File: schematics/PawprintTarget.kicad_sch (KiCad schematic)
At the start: 47 parts, among them J1 Conn_01x15, J2 Conn_01x15, J4 RJ45, J5 RJ45, J8 Conn_01x04_Pin, J9 Conn_01x04_Pin, Q1 IRF540N, Q2 IRF540N, SW1 SW_DIP_x04, SW2 SW_DIP_x04, U1 MAX485E, U2 TSOP38G36, U3 Mini360

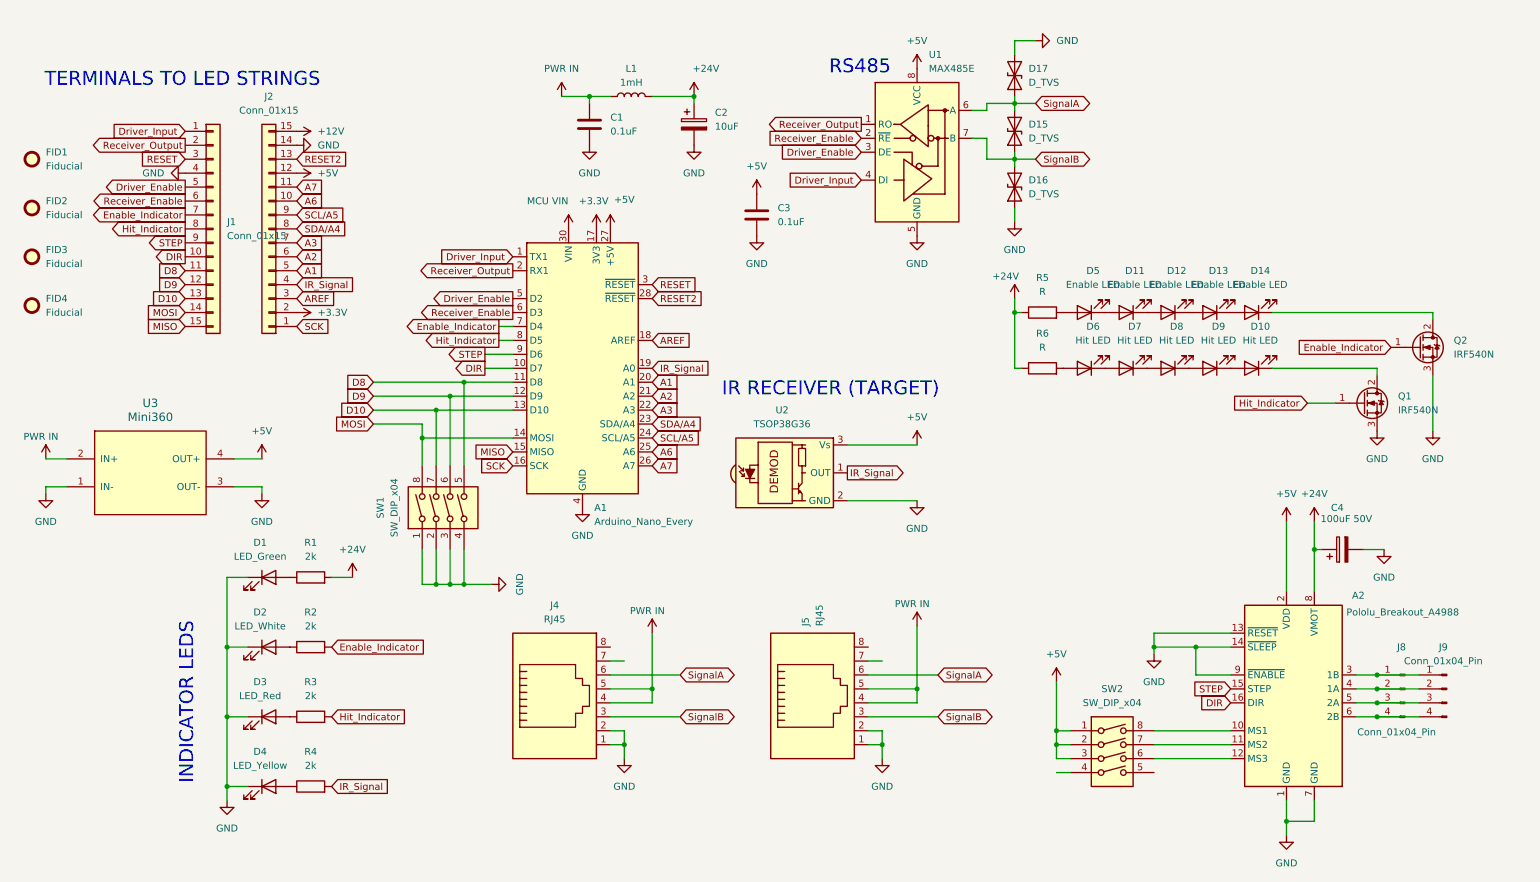
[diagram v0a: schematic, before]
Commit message: Component placements finished
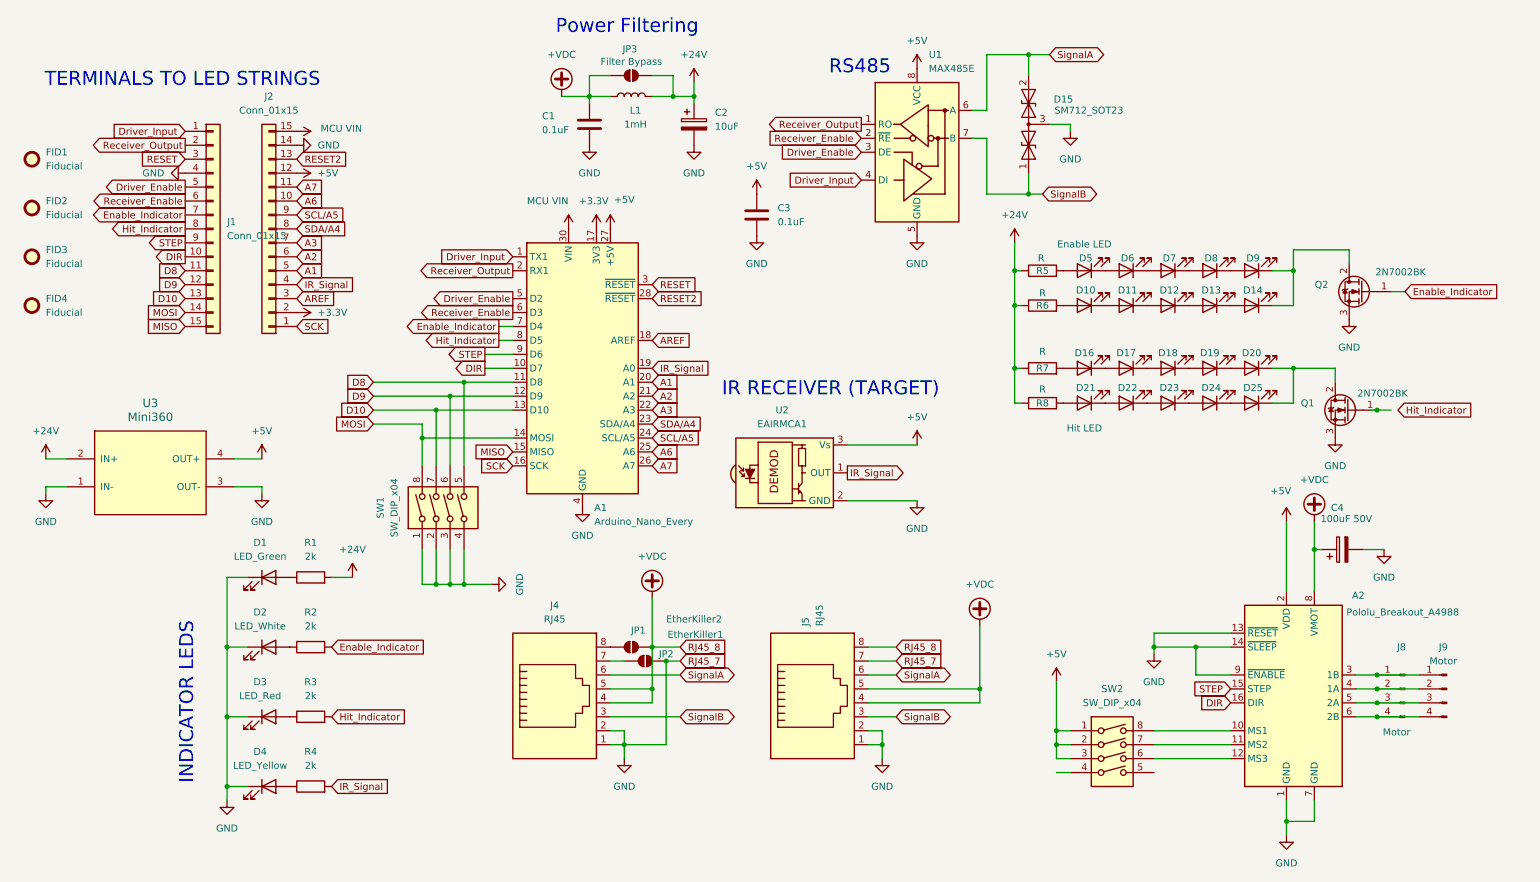
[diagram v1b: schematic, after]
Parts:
- removed D15, D16, D17: D_TVS, symbol Device:D_TVS
- added D10, D11, D12, D13, D14: Enable LED, LED_SMD:LED_1206_3216Metric, symbol Device:LED
- added D15: SM712_SOT23, Package_TO_SOT_SMD:SOT-23, symbol Diode:SM712_SOT23
- added D21, D22, D23, D24, D25: Hit LED, LED_SMD:LED_1206_3216Metric, symbol Device:LED
- added JP1: EtherKiller1, Jumper:SolderJumper-2_P1.3mm_Open_TrianglePad1.0x1.5mm, symbol Jumper:SolderJumper_2_Open
- added JP2: EtherKiller2, Jumper:SolderJumper-2_P1.3mm_Open_TrianglePad1.0x1.5mm, symbol Jumper:SolderJumper_2_Open
- added JP3: Filter Bypass, Jumper:SolderJumper-2_P1.3mm_Open_TrianglePad1.0x1.5mm, symbol Jumper:SolderJumper_2_Open
- added R6, R8: R, Resistor_SMD:R_0603_1608Metric, symbol Device:R
- C1, C3: footprint Capacitor_THT:C_Disc_D3.0mm_W2.0mm_P2.50mm -> Capacitor_SMD:C_0805_2012Metric
- C2: footprint Capacitor_THT:CP_Radial_D5.0mm_P2.00mm -> Capacitor_SMD:C_1206_3216Metric
- J8: value Conn_01x04_Pin -> Motor
- J9: value Conn_01x04_Pin -> Motor; footprint Connector_PinSocket_2.54mm:PinSocket_1x04_P2.54mm_Vertical -> Connector_JST:JST_PH_B4B-PH-K_1x04_P2.00mm_Vertical
- L1: footprint Inductor_THT:L_Radial_D9.5mm_P5.00mm_Fastron_07HVP -> Mini360_step-down:Inductor_SDR1307
- Q1, Q2: value IRF540N -> 2N7002BK; footprint Package_TO_SOT_THT:TO-220-3_Vertical -> Package_TO_SOT_SMD:SOT-23-3
- R1, R2, R3, R4: footprint Resistor_SMD:R_1210_3225Metric -> Resistor_SMD:R_0603_1608Metric
- U2: value TSOP38G36 -> EAIRMCA1; footprint OptoDevice:Vishay_MINICAST-3Pin -> OptoDevice:Vishay_MOLD-3Pin
- renumbered D6 to D16, D7 to D17, D8 to D18, D9 to D19, D10 to D20, D11 to D6, D12 to D7, D13 to D8, D14 to D9, R6 to R7
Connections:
- net +12V is gone; now on net MCU VIN: J2.15 (Pin_15)
- net +24V: now also U3.2 (IN+), JP3.2 (B), R6.1, R8.1; no longer A2.8 (VMOT), C4.1
- net GND: now also J5.7, D15.3 (common), JP1.2 (B)
- net Hit_Indicator: no longer Q1.1 (G)
- net SignalA: now also D15.2 (A2)
- net SignalB: now also D15.1 (A1)
- net at J4.7: now also JP1.1 (A)
- net at J4.8: now also JP2.1 (A)
- net at D9.1 (K), Q2.2 (D): now also D14.1 (K)
- net +VDC: now reaches J5.8
- net +VDC: now also A2.8 (VMOT), C1.1, C4.1, J4.4, J4.5, J5.4, J5.5, L1.1, JP2.2 (B), JP3.1 (A)
- net at D20.1 (K), Q1.2 (D): now also D25.1 (K)
- removed net PWR IN: C1.1, J4.4, J4.5, J5.4, J5.5, L1.1, U3.2 (IN+)
- new net: D12.1 (K), D13.2 (A)
- new net: D11.1 (K), D12.2 (A)
- new net: D23.1 (K), D24.2 (A)
- new net: D22.1 (K), D23.2 (A)
- new net: D21.1 (K), D22.2 (A)
- new net: D21.2 (A), R8.2
- new net: D10.2 (A), R6.2
- new net: D10.1 (K), D11.2 (A)
- new net: D13.1 (K), D14.2 (A)
- new net: D24.1 (K), D25.2 (A)
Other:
- note added: "Power Filtering"
- moved on the sheet: D5, D6, D7, D8, D9, Q1, Q2, R5

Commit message: Fix RJ45 connector
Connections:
- net +VDC: no longer J5.8
- net GND: no longer J5.7
- net RJ45_7: now reaches J4.7, JP1.1 (A)
- net RJ45_7: now also J5.7
- net RJ45_8: now reaches J4.8, JP2.1 (A)
- net RJ45_8: now also J5.8
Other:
- moved on the sheet: JP1, JP2

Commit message: Done, probably
- Nicer labels
- Probably won't blow up
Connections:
- net Hit_Indicator: now also Q1.1 (G)
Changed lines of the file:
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@@
-	)
-	(junction
-		(at 264.16 85.09)
-		(diameter 0)
-		(color 0 0 0 0)
 	)
 	(junction
@@
 	(wire
 		(pts
-			(xy 264.16 85.09) (xy 262.89 85.09)
-		)
-		(stroke
-			(width 0)
-			(type default)
-		)
-	)
-	(wire
-		(pts
 			(xy 54.61 153.67) (xy 58.42 153.67)
 		)
@@
 	(wire
 		(pts
+			(xy 264.16 85.09) (xy 267.97 85.09)
+		)
+		(stroke
+			(width 0)
+			(type default)
+		)
+	)
+	(wire
+		(pts
 			(xy 58.42 115.57) (xy 54.61 115.57)
 		)
@@
 		)
 		(stroke
-			(width 0)
-			(type default)
-		)
-	)
-	(wire
-		(pts
-			(xy 266.7 85.09) (xy 264.16 85.09)
-		)
-		(stroke

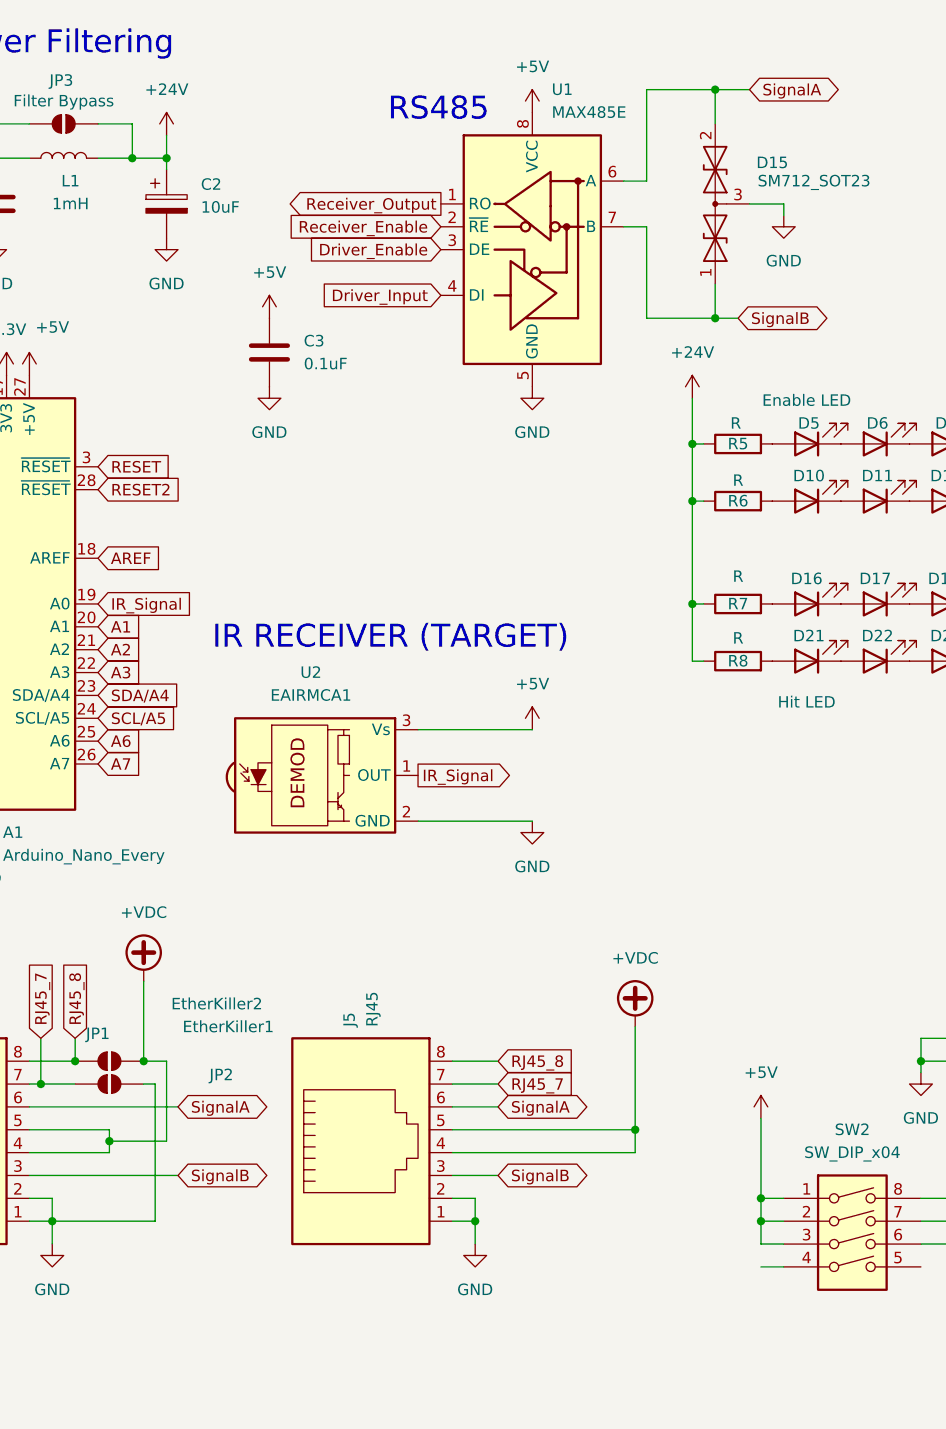
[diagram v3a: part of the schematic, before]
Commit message: Fix ERC errors
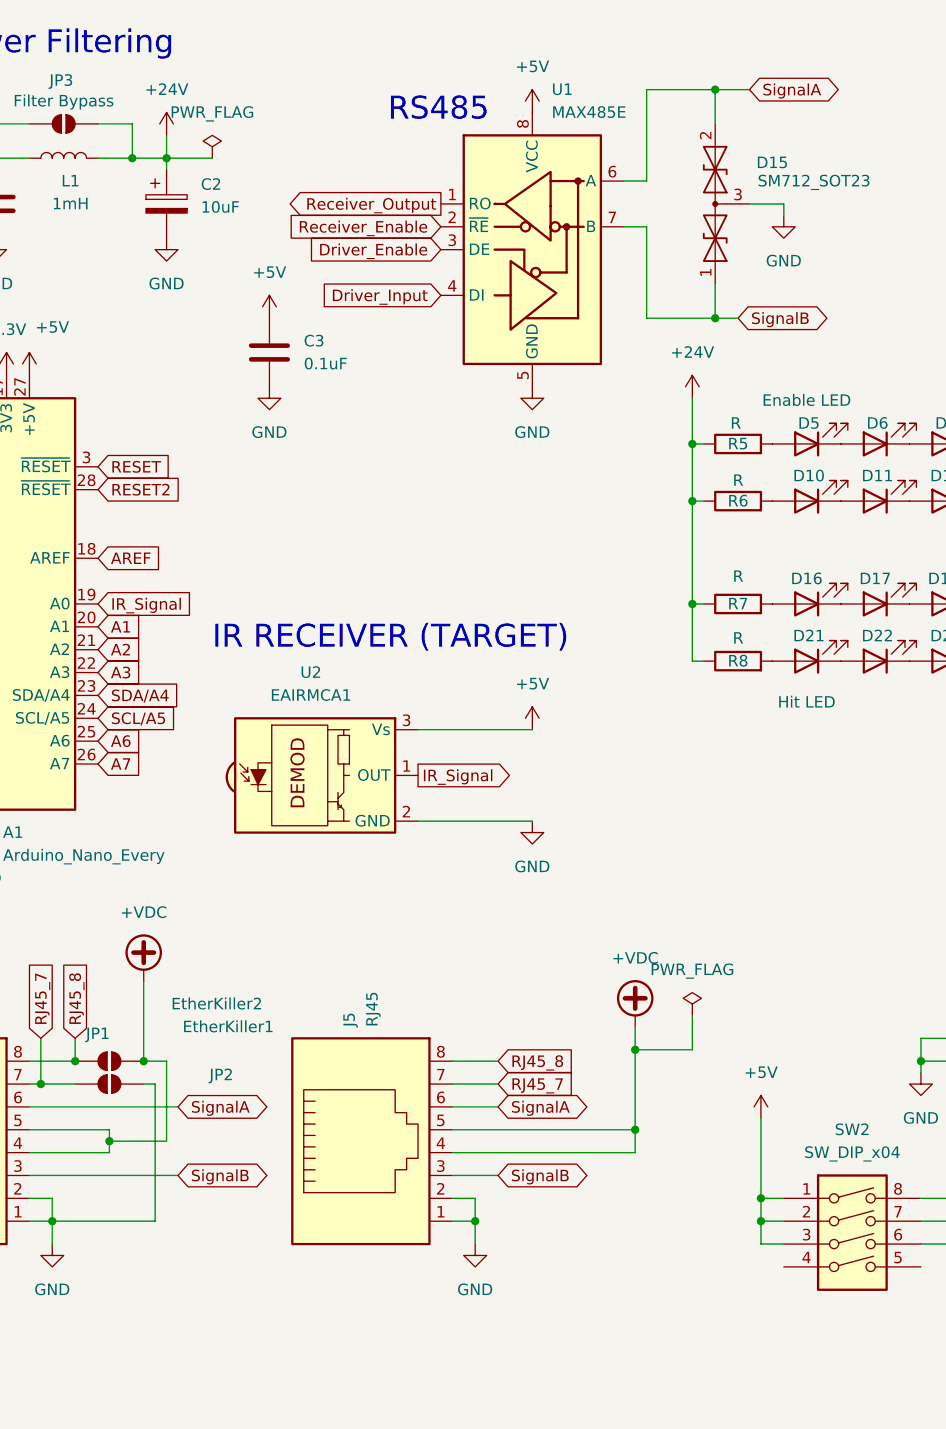
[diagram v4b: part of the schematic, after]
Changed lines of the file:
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@@
 	)
 	(junction
+		(at 191.77 127)
+		(diameter 0)
+		(color 0 0 0 0)
+	)
+	(junction
 		(at 198.12 77.47)
 		(diameter 0)
@@
 	(wire
 		(pts
+			(xy 198.12 123.19) (xy 198.12 127)
+		)
+		(stroke
+			(width 0)
+			(type default)
+		)
+	)
+	(wire
+		(pts
 			(xy 92.71 85.09) (xy 92.71 95.25)
 		)
@@
 	(wire
 		(pts
+			(xy 191.77 127) (xy 191.77 135.89)
+		)
+		(stroke
+			(width 0)
+			(type default)
+		)
+	)
+	(wire
+		(pts
 			(xy 252.73 110.49) (xy 254 110.49)
 		)
@@
 	(wire
 		(pts
+			(xy 198.12 127) (xy 191.77 127)
+		)
+		(stroke
+			(width 0)
+			(type default)
+		)
+	)
+	(wire
+		(pts
 			(xy 198.12 54.61) (xy 198.12 59.69)
 		)
@@
 	(wire
 		(pts
-			(xy 208.28 151.13) (xy 205.74 151.13)
-		)
-		(stroke
-			(width 0)
-			(type default)
-		)
-	)
-	(wire
-		(pts
 			(xy 248.92 77.47) (xy 256.54 77.47)
 		)
@@
 	(wire
 		(pts
+			(xy 139.7 27.94) (xy 144.78 27.94)
+		)
+		(stroke
+			(width 0)
+			(type default)
+		)
+	)
+	(wire
+		(pts
 			(xy 97.79 116.84) (xy 95.25 116.84)
 		)
@@
 	(wire
 		(pts
-			(xy 191.77 124.46) (xy 191.77 135.89)
+			(xy 191.77 124.46) (xy 191.77 127)
 		)
 		(stroke
@@
 	)
 	(symbol
+		(lib_id "power:PWR_FLAG")
+		(at 198.12 123.19 0)
+		(unit 1)
+		(exclude_from_sim no)
+		(in_bom yes)
+		(on_board yes)
+		(dnp no)
+		(fields_autoplaced yes)
+		(property "Reference" "#FLG01"
+			(at 198.12 121.285 0)
+			(effects
+				(font
+					(size 1.27 1.27)
+				)
+				(hide yes)
+			)
+		)
+		(property "Value" "PWR_FLAG"
+			(at 198.12 118.11 0)
+			(effects
+				(font
+					(size 1.27 1.27)
+				)
+			)
+		)
+		(property "Footprint" ""
+			(at 198.12 123.19 0)
+			(effects
+				(font
+					(size 1.27 1.27)
+				)
+				(hide yes)
+			)
+		)
+		(property "Datasheet" "~"
+			(at 198.12 123.19 0)
+			(effects
+				(font
+					(size 1.27 1.27)
+				)
+				(hide yes)
+			)
+		)
+		(property "Description" "Special symbol for telling ERC where power comes from"
+			(at 198.12 123.19 0)
+			(effects
+				(font
+					(size 1.27 1.27)
+				)
+				(hide yes)
+			)
+		)
+		(pin "1"
+		)
+		(instances
+			(project ""
+				(path "/bf8ec27c-ff5f-49a5-86e3-ca23713e8dc9"
+					(reference "#FLG01")
+					(unit 1)
+				)
+			)
+		)
+	)
+	(symbol
 		(lib_id "power:GND")
 		(at 256.54 90.17 0)
@@
 					(unit 1)
 				)
+			)
+		)
+	)
+	(symbol
+		(lib_id "power:PWR_FLAG")
+		(at 144.78 27.94 0)
+		(unit 1)
+		(exclude_from_sim no)
+		(in_bom yes)
+		(on_board yes)
+		(dnp no)
+		(fields_autoplaced yes)
+		(property "Reference" "#FLG02"
+			(at 144.78 26.035 0)
+			(effects
+				(font
+					(size 1.27 1.27)
+				)
+				(hide yes)
+			)
+		)
+		(property "Value" "PWR_FLAG"
+			(at 144.78 22.86 0)
+			(effects
+				(font
+					(size 1.27 1.27)
+				)
+			)
+		)
+		(property "Footprint" ""
+			(at 144.78 27.94 0)
+			(effects
+				(font
+					(size 1.27 1.27)
+				)
+				(hide yes)
+			)
+		)
+		(property "Datasheet" "~"
+			(at 144.78 27.94 0)
+			(effects
+				(font
+					(size 1.27 1.27)
+				)
+				(hide yes)
+			)
+		)
+		(property "Description" "Special symbol for telling ERC where power comes from"
+			(at 144.78 27.94 0)
+			(effects
+				(font
+					(size 1.27 1.27)
+				)
+				(hide yes)
+			)
+		)
+		(pin "1"
+		)
+		(instances
+			(project "PawprintTarget"
+				(path "/bf8ec27c-ff5f-49a5-86e3-ca23713e8dc9"
+					(reference "#FLG02")
+					(unit 1)
+				)

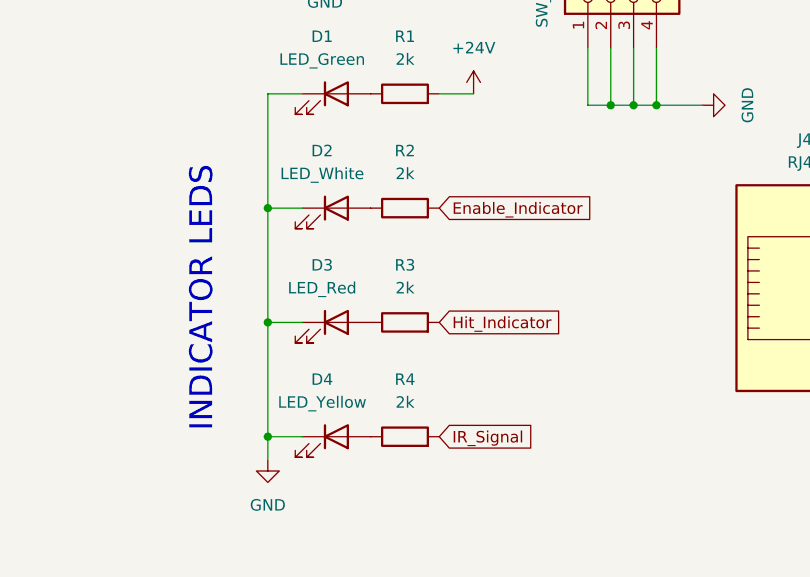
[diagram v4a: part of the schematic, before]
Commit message: Add panelized version, revise LED resistor values
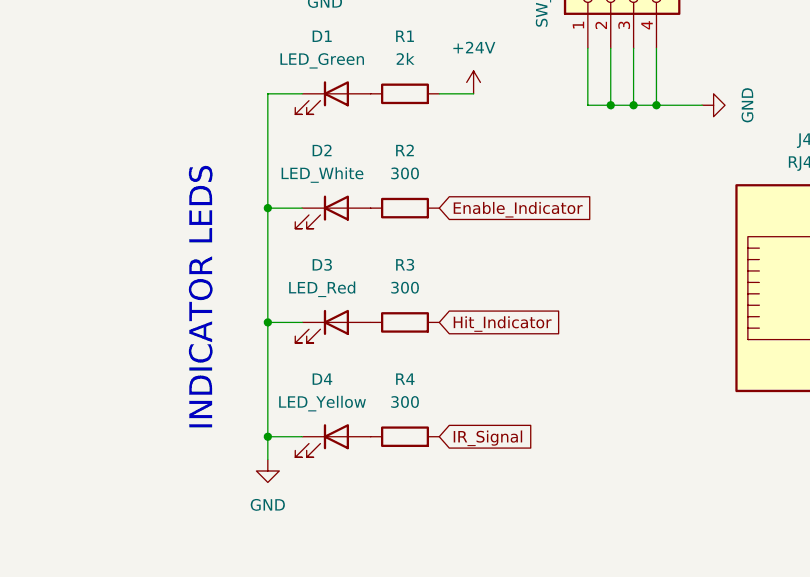
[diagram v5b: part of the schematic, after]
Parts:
- R2, R3, R4: value 2k -> 300
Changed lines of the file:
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@@
 			)
 		)
-		(property "Value" "2k"
+		(property "Value" "300"
 			(at 69.85 137.16 90)
 			(effects
@@
 			)
 		)
-		(property "Value" "2k"
+		(property "Value" "300"
 			(at 69.85 124.46 90)
 			(effects
@@
 			)
 		)
-		(property "Value" "2k"
+		(property "Value" "300"
 			(at 69.85 149.86 90)
 			(effects
